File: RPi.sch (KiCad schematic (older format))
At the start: 4 parts, among them U3 LMS6002DR2, U4 ECP5, X3 RaspberryPiConnector

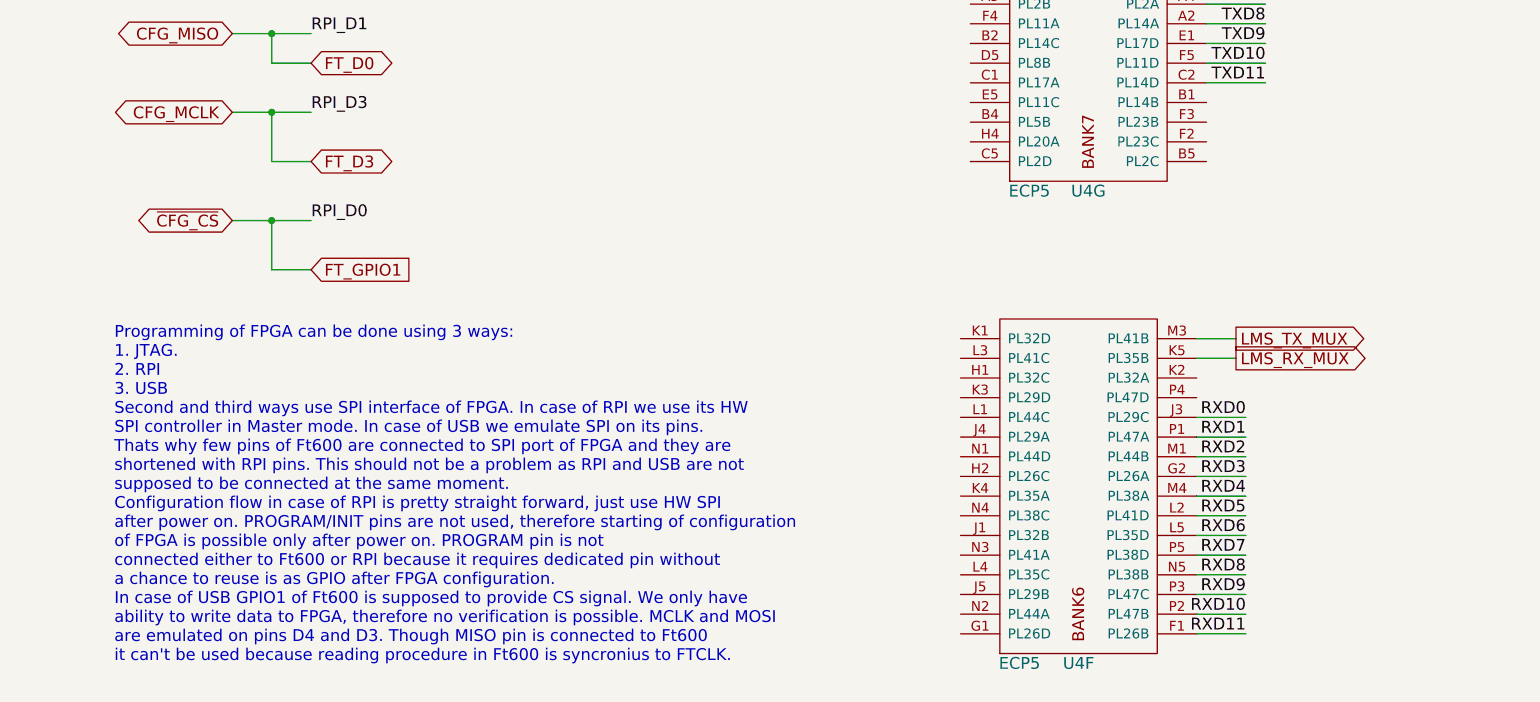
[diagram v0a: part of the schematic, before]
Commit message: Add leds. Traced LMS_3V3A LDO.
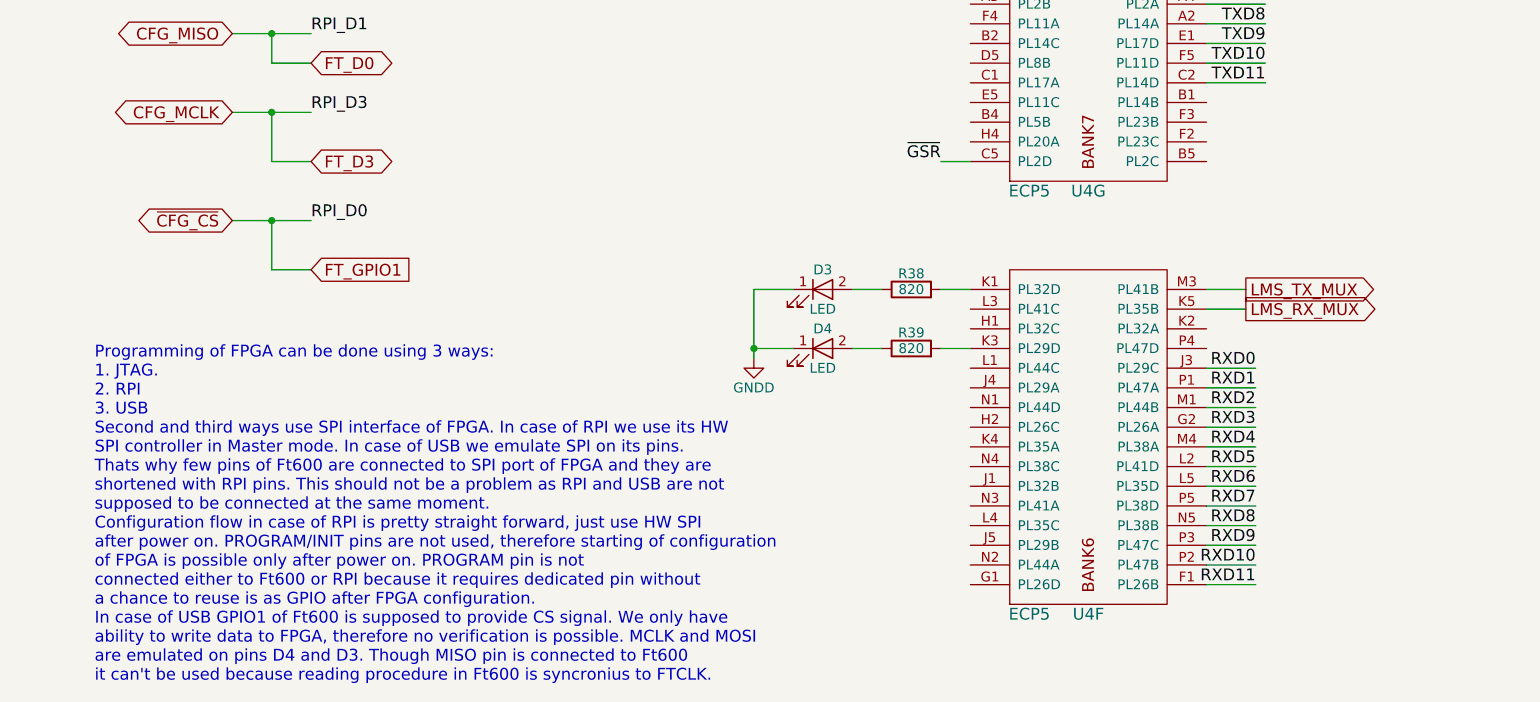
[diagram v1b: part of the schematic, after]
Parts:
- added D3, D4: LED, symbol LED
- added R38, R39: 820, symbol R
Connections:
- net GNDD: now also D3.1 (K), D4.1 (K)
- net at U4.K1 (PL32D): now also R38.2
- net at U4.K3 (PL29D): now also R39.2
- net ~GSR: now reaches U4.C5 (PL2D)
- new net: D4.2 (A), R39.1
- new net: D3.2 (A), R38.1
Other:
- moved on the sheet: U4F
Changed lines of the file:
@@
 $EndComp
 $Comp
-L +3V3 #PWR038
+L +3V3 #PWR037
 U 1 1 58A418F6
 P 800 1250
-F 0 "#PWR038" H 800 1100 50  0001 C CNN
+F 0 "#PWR037" H 800 1100 50  0001 C CNN
 F 1 "+3V3" H 800 1390 50  0000 C CNN
 F 2 "" H 800 1250 50  0000 C CNN
@@
 $EndComp
 $Comp
-L GNDD #PWR039
+L GNDD #PWR038
 U 1 1 58A80C0C
 P 1400 2500
-F 0 "#PWR039" H 1400 2250 50  0001 C CNN
+F 0 "#PWR038" H 1400 2250 50  0001 C CNN
 F 1 "GNDD" H 1400 2350 50  0000 C CNN
 F 2 "" H 1400 2500 50  0000 C CNN
@@
 	1600 5050 1600 4800
 Connection ~ 1600 4800
-Text Notes 800  7600 0    60   ~ 0
+Text Notes 700  7700 0    60   ~ 0
 Programming of FPGA can be done using 3 ways:\n1. JTAG. \n2. RPI\n3. USB\nSecond and third ways use SPI interface of FPGA. In case of RPI we use its HW\nSPI controller in Master mode. In case of USB we emulate SPI on its pins.\nThats why few pins of Ft600 are connected to SPI port of FPGA and they are\nshortened with RPI pins. This should not be a problem as RPI and USB are not\nsupposed to be connected at the same moment.\nConfiguration flow in case of RPI is pretty straight forward, just use HW SPI\nafter power on. PROGRAM/INIT pins are not used, therefore starting of configuration \nof FPGA is possible only after power on. PROGRAM pin is not\nconnected either to Ft600 or RPI because it requires dedicated pin without\na chance to reuse is as GPIO after FPGA configuration.\nIn case of USB GPIO1 of Ft600 is supposed to provide CS signal. We only have\nability to write data to FPGA, therefore no verification is possible. MCLK and MOSI \nare emulated on pins D4 and D3. Though MISO pin is connected to Ft600 \nit can't be used because reading procedure in Ft600 is syncronius to FTCLK.\n
 $Comp
 L ECP5 U4
 U 6 1 592480E1
-P 5300 7550
-F 0 "U4" H 5700 7500 60  0000 C CNN
-F 1 "ECP5" H 5400 7500 60  0000 C CNN
-F 2 "sdr-foots:ECP5_381" H 3750 8100 60  0001 C CNN
-F 3 "" H 3750 8100 60  0001 C CNN
-	6    5300 7550
+P 5350 7300
+F 0 "U4" H 5750 7250 60  0000 C CNN
+F 1 "ECP5" H 5450 7250 60  0000 C CNN
+F 2 "sdr-foots:ECP5_381" H 3800 7850 60  0001 C CNN
+F 3 "" H 3800 7850 60  0001 C CNN
+	6    5350 7300
 	1    0    0    -1
 $EndComp
@@
 	1    0    0    -1
 $EndComp
-Text GLabel 6500 5950 2    60   Output ~ 0
+Text GLabel 6550 5700 2    60   Output ~ 0
 LMS_TX_MUX
-Text GLabel 6500 6050 2    60   Output ~ 0
+Text GLabel 6550 5800 2    60   Output ~ 0
 LMS_RX_MUX
 Wire Wire Line
-	6500 5950 6300 5950
+	6550 5700 6350 5700
 Text Label 6650 3550 2    60   ~ 0
 TXD0
@@
 Wire Wire Line
 	6350 4650 6650 4650
-Text Label 6550 6350 2    60   ~ 0
+Text Label 6600 6100 2    60   ~ 0
 RXD0
-Text Label 6550 6450 2    60   ~ 0
+Text Label 6600 6200 2    60   ~ 0
 RXD1
-Text Label 6550 6550 2    60   ~ 0
+Text Label 6600 6300 2    60   ~ 0
 RXD2
-Text Label 6550 6650 2    60   ~ 0
+Text Label 6600 6400 2    60   ~ 0
 RXD3
-Text Label 6550 6750 2    60   ~ 0
+Text Label 6600 6500 2    60   ~ 0
 RXD4
-Text Label 6550 6850 2    60   ~ 0
+Text Label 6600 6600 2    60   ~ 0
 RXD5
-Text Label 6550 6950 2    60   ~ 0
+Text Label 6600 6700 2    60   ~ 0
 RXD6
-Text Label 6550 7050 2    60   ~ 0
+Text Label 6600 6800 2    60   ~ 0
 RXD7
-Text Label 6550 7150 2    60   ~ 0
+Text Label 6600 6900 2    60   ~ 0
 RXD8
-Text Label 6550 7250 2    60   ~ 0
+Text Label 6600 7000 2    60   ~ 0
 RXD9
-Text Label 6550 7350 2    60   ~ 0
+Text Label 6600 7100 2    60   ~ 0
 RXD10
-Text Label 6550 7450 2    60   ~ 0
+Text Label 6600 7200 2    60   ~ 0
 RXD11
 Wire Wire Line
-	6550 6350 6300 6350
-Wire Wire Line
-	6550 6450 6300 6450
-Wire Wire Line
-	6550 6550 6300 6550
-Wire Wire Line
-	6550 6650 6300 6650
-Wire Wire Line
-	6550 6750 6300 6750
-Wire Wire Line
-	6550 6850 6300 6850
-Wire Wire Line
-	6550 6950 6300 6950
-Wire Wire Line
-	6550 7050 6300 7050
-Wire Wire Line
-	6550 7150 6300 7150
-Wire Wire Line
-	6550 7250 6300 7250
-Wire Wire Line
-	6550 7350 6300 7350
-Wire Wire Line
-	6550 7450 6300 7450
-Wire Wire Line
-	6500 6050 6300 6050
+	6600 6100 6350 6100
+Wire Wire Line
+	6600 6200 6350 6200
+Wire Wire Line
+	6600 6300 6350 6300
+Wire Wire Line
+	6600 6400 6350 6400
+Wire Wire Line
+	6600 6500 6350 6500
+Wire Wire Line
+	6600 6600 6350 6600
+Wire Wire Line
+	6600 6700 6350 6700
+Wire Wire Line
+	6600 6800 6350 6800
+Wire Wire Line
+	6600 6900 6350 6900
+Wire Wire Line
+	6600 7000 6350 7000
+Wire Wire Line
+	6600 7100 6350 7100
+Wire Wire Line
+	6600 7200 6350 7200
+Wire Wire Line
+	6550 5800 6350 5800
 $Comp
 L LMS6002DR2 U3
@@
 Wire Wire Line
 	8850 4000 9100 4000
+$Comp
+L LED D4
+U 1 1 5938F77D
+P 4400 6000
+F 0 "D4" H 4400 6100 50  0000 C CNN
+F 1 "LED" H 4400 5900 50  0000 C CNN
+F 2 "" H 4400 6000 50  0001 C CNN
+F 3 "" H 4400 6000 50  0001 C CNN
+	1    4400 6000
+	1    0    0    -1
+$EndComp
+$Comp
+L LED D3
+U 1 1 5938F8CC
+P 4400 5700
+F 0 "D3" H 4400 5800 50  0000 C CNN
+F 1 "LED" H 4400 5600 50  0000 C CNN
+F 2 "" H 4400 5700 50  0001 C CNN
+F 3 "" H 4400 5700 50  0001 C CNN
+	1    4400 5700
+	1    0    0    -1
+$EndComp
+$Comp
+L R R38
+U 1 1 5938F9AA
+P 4850 5700
+F 0 "R38" V 4930 5700 50  0000 C CNN
+F 1 "820" V 4850 5700 50  0000 C CNN
+F 2 "" V 4780 5700 50  0001 C CNN
+F 3 "" H 4850 5700 50  0001 C CNN
+	1    4850 5700
+	0    -1   -1   0
+$EndComp
+$Comp
+L R R39
+U 1 1 5938F9FB
+P 4850 6000
+F 0 "R39" V 4930 6000 50  0000 C CNN
+F 1 "820" V 4850 6000 50  0000 C CNN
+F 2 "" V 4780 6000 50  0001 C CNN
+F 3 "" H 4850 6000 50  0001 C CNN
+	1    4850 6000
+	0    -1   -1   0
+$EndComp
+Wire Wire Line
+	5150 5700 5000 5700
+Wire Wire Line
+	5000 6000 5150 6000
+Wire Wire Line
+	4700 6000 4550 6000
+Wire Wire Line
+	4700 5700 4550 5700
+$Comp
+L GNDD #PWR039
+U 1 1 5938FEB2
+P 4050 6050
+F 0 "#PWR039" H 4050 5800 50  0001 C CNN
+F 1 "GNDD" H 4050 5900 50  0000 C CNN
+F 2 "" H 4050 6050 50  0001 C CNN
+F 3 "" H 4050 6050 50  0001 C CNN
+	1    4050 6050
+	1    0    0    -1
+$EndComp
+Wire Wire Line
+	4250 6000 4050 6000
+Wire Wire Line
+	4050 5700 4050 6050
+Wire Wire Line
+	4250 5700 4050 5700
+Connection ~ 4050 6000
+Text Label 5000 5050 2    60   ~ 0
+~GSR
+Wire Wire Line
+	5150 5050 5000 5050
 $EndSCHEMATC
